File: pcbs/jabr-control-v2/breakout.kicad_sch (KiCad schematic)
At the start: 0 parts

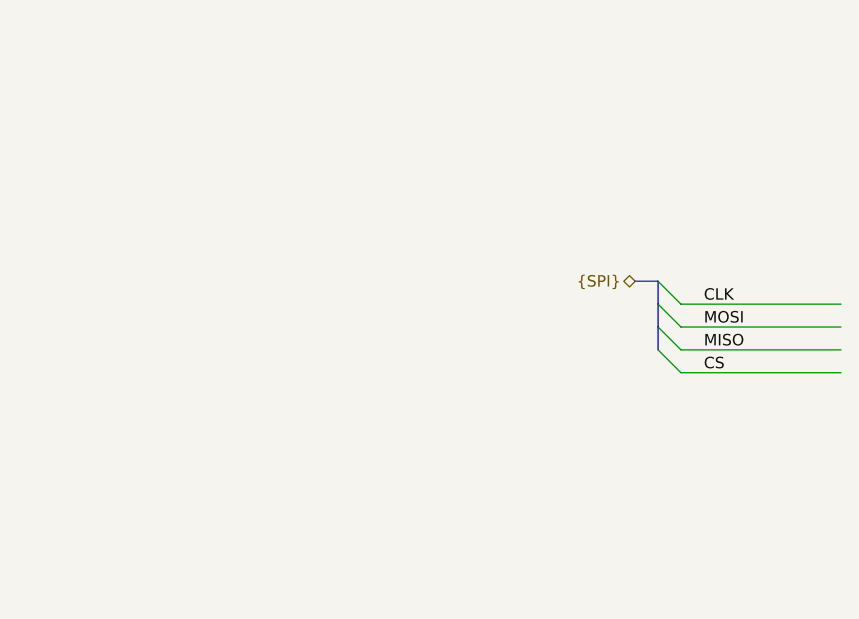
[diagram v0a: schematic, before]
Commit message: Removed power button reset to switch (power will be cycled anyway)
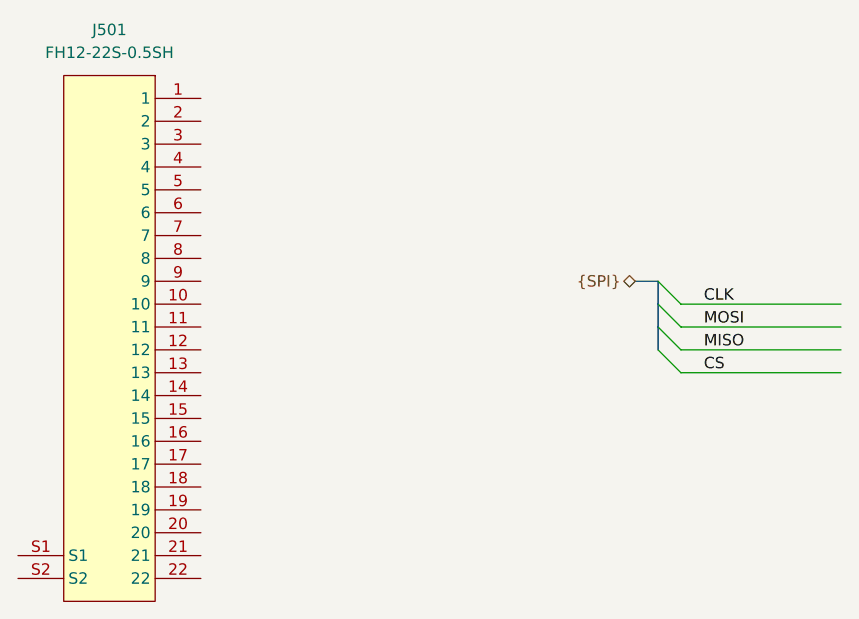
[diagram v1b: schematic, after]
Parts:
- added J501: FH12-22S-0.5SH, project_footprints:Hirose_FH12-22S-0.5SH_1x22-1MP_P0.50mm_Horizontal, symbol CONN-FPC:FH12-22S-0.5SH
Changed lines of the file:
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@@
+		)
+	)
+	(symbol
+		(lib_id "CONN-FPC:FH12-22S-0.5SH")
+		(at 81.28 68.58 0)
+		(mirror y)
+		(unit 1)
+		(body_style 1)
+		(exclude_from_sim no)
+		(in_bom yes)
+		(on_board yes)
+		(in_pos_files yes)
+		(dnp no)
+		(fields_autoplaced yes)
+		(property "Reference" "J501"
+			(at 81.28 63.5 0)
+			(show_name no)
+			(do_not_autoplace no)
+			(effects
+				(font
+					(size 1.27 1.27)
+				)
+			)
+		)
+		(property "Value" "FH12-22S-0.5SH"
+			(at 81.28 66.04 0)
+			(show_name no)
+			(do_not_autoplace no)
+			(effects
+				(font
+					(size 1.27 1.27)
+				)
+			)
+		)
+		(property "Footprint" "project_footprints:Hirose_FH12-22S-0.5SH_1x22-1MP_P0.50mm_Horizontal"
+			(at 80.01 132.08 0)
+			(hide yes)
+			(show_name no)
+			(do_not_autoplace no)
+			(effects
+				(font
+					(size 1.27 1.27)
+				)
+			)
+		)
+		(property "Datasheet" "https://www.mouser.co.uk/datasheet/3/731/1/FH12_22S_0.5SH_55_CL0586_0532_7_55_2DDrawing_0000987484.pdf"
+			(at 81.28 129.54 0)
+			(hide yes)
+			(show_name no)
+			(do_not_autoplace no)
+			(effects
+				(font
+					(size 1.27 1.27)
+				)
+			)
+		)
+		(property "Description" ""
+			(at 81.28 68.58 0)
+			(hide yes)
+			(show_name no)
+			(do_not_autoplace no)
+			(effects
+				(font
+					(size 1.27 1.27)
+				)
+			)
+		)
+		(property "Field6" ""
+			(at 81.28 68.58 0)
+			(hide yes)
+			(show_name no)
+			(do_not_autoplace no)
+			(effects
+				(font
+					(size 1.27 1.27)
+				)
+			)
+		)
+		(property "Field7" ""
+			(at 81.28 68.58 0)
+			(hide yes)
+			(show_name no)
+			(do_not_autoplace no)
+			(effects
+				(font
+					(size 1.27 1.27)
+				)
+			)
+		)
+		(property "Part Description" ""
+			(at 81.28 68.58 0)
+			(hide yes)
+			(show_name no)
+			(do_not_autoplace no)
+			(effects
+				(font
+					(size 1.27 1.27)
+				)
+			)
+		)
+		(pin "7"
+		)
+		(pin "22"
+		)
+		(pin "4"
+		)
+		(pin "2"
+		)
+		(pin "15"
+		)
+		(pin "S2"
+		)
+		(pin "12"
+		)
+		(pin "6"
+		)
+		(pin "1"
+		)
+		(pin "9"
+		)
+		(pin "16"
+		)
+		(pin "14"
+		)
+		(pin "17"
+		)
+		(pin "13"
+		)
+		(pin "3"
+		)
+		(pin "5"
+		)
+		(pin "8"
+		)
+		(pin "18"
+		)
+		(pin "11"
+		)
+		(pin "19"
+		)
+		(pin "20"
+		)
+		(pin "21"
+		)
+		(pin "10"
+		)
+		(pin "S1"
+		)
+		(instances
+			(project "jabr-control-v2"
+				(path "/f91ec272-d09a-4038-bbbb-962739a92c51/25c588fa-eee6-4ec0-9367-0f9042b543c0"
+					(reference "J501")
+					(unit 1)
+				)
+			)
 		)
 	)

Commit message: Schematic done
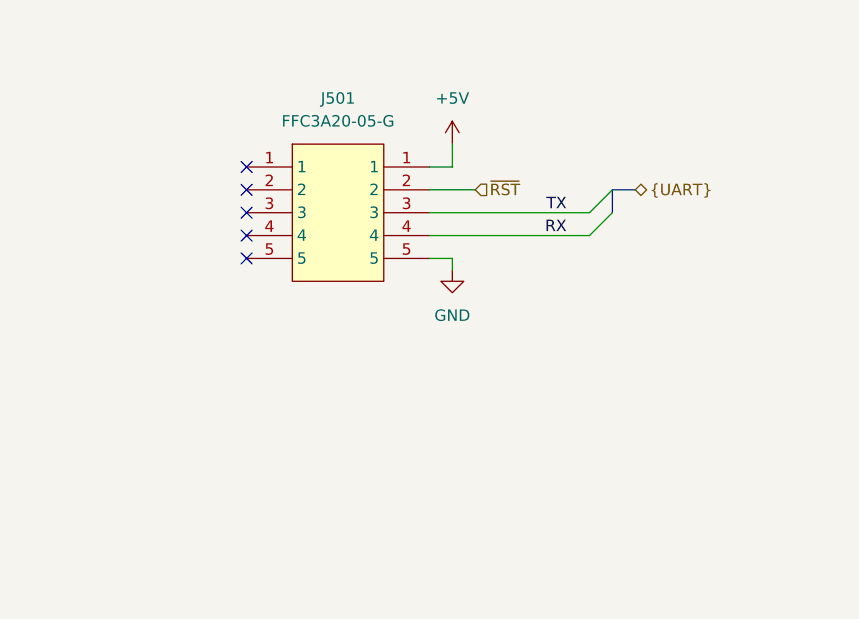
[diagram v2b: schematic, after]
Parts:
- removed J501: FH12-22S-0.5SH, project_footprints:Hirose_FH12-22S-0.5SH_1x22-1MP_P0.50mm_Horizontal, symbol CONN-FPC:FH12-22S-0.5SH
- added J501: FFC3A20-05-G, project_footprints:FFC3A2005G, symbol CONN-FPC:FFC3A20-05-G
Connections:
- new net +5V: J501.1
- new net GND: J501.5
- new net RX: J501.4
- new net TX: J501.3
- new net ~{RST}: J501.2
- no-connect marks 0 -> 5
